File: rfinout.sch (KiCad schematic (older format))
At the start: 4 parts, among them K7 ANT_RLY, P4 ANT, P5 RADIO, P6 PTT_IN

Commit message: All layed out
Several net errors fixed, and some mcu pins reassigned for better layout.
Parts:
- removed K7: ANT_RLY, nu9j-footprints:EC2-12NU, symbol RELAY_2RT
- added K7: ANT_RLY, symbol RELAY_2RT-KEMET
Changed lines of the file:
@@
 Text HLabel 6250 2500 2    60   Output ~ 0
 ptt
+Text Notes 3050 3600 0    60   ~ 0
+SMA Connectors: Johnson 142-0701-801
 $Comp
-L RELAY_2RT K7
-U 1 1 547A886B
+L RELAY_2RT-KEMET K7
+U 1 1 54849E97
 P 6350 3700
 F 0 "K7" H 6300 4100 70  0000 C CNN
 F 1 "ANT_RLY" H 6500 3200 70  0000 C CNN
-F 2 "nu9j-footprints:EC2-12NU" H 6350 3700 60  0001 C CNN
+F 2 "" H 6350 3700 60  0000 C CNN
 F 3 "" H 6350 3700 60  0000 C CNN
 	1    6350 3700
 	1    0    0    -1
 $EndComp
-Text Notes 3050 3600 0    60   ~ 0
-SMA Connectors: Johnson 142-0701-801
 $EndSCHEMATC

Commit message: Connected all mcu VSS and VDD pins.
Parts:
- K7: footprint (none) -> nu9j-footprints:EC2-12NU
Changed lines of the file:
@@
 F 0 "K7" H 6300 4100 70  0000 C CNN
 F 1 "ANT_RLY" H 6500 3200 70  0000 C CNN
-F 2 "" H 6350 3700 60  0000 C CNN
+F 2 "nu9j-footprints:EC2-12NU" H 6350 3700 60  0001 C CNN
 F 3 "" H 6350 3700 60  0000 C CNN
 	1    6350 3700

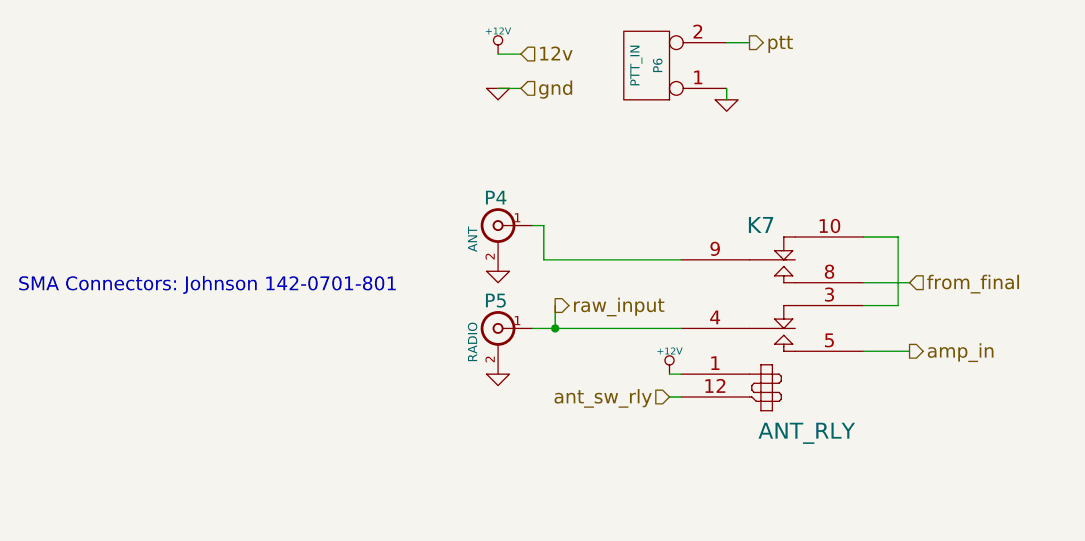
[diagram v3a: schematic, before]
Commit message: Fixed issues found with test board
- Added MOSFETs to relay switch lines from MCU
- Reconnected SWR in/out to actual ADC pins
- Changed LM3940 footprint to SOT223
- Added 4th mounting hole
- Swapped joystick for nav button
- Extended pads of STM32F401 for easier soldering
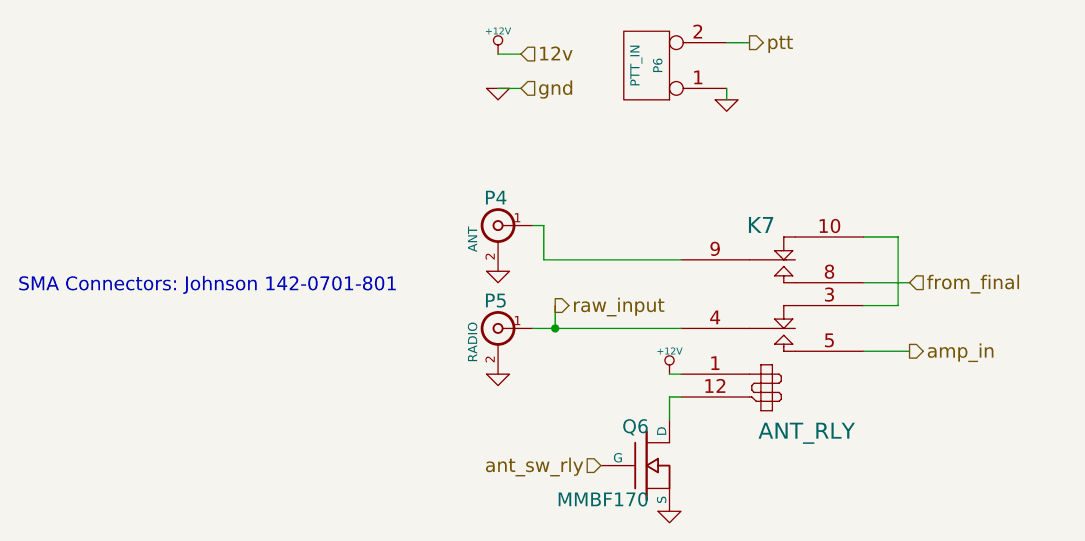
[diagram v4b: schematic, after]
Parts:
- added Q6: MMBF170, nu9j-footprints:sot23-DGS, symbol MOSFET_N
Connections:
- net GND: now also Q6.S
- net ant_sw_rly: now also Q6.G; no longer K7.12
- new net: K7.12, Q6.D
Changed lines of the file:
@@
 $EndComp
 $Comp
-L +12V #PWR098
+L +12V #PWR0101
 U 1 1 5472C39F
 P 5900 3950
-F 0 "#PWR098" H 5900 3900 20  0001 C CNN
+F 0 "#PWR0101" H 5900 3900 20  0001 C CNN
 F 1 "+12V" H 5900 4050 30  0000 C CNN
 F 2 "" H 5900 3950 60  0000 C CNN
@@
 Wire Wire Line
 	5950 4050 5900 4050
-Text HLabel 5900 4050 0    60   Input ~ 0
+Text HLabel 5600 4350 0    60   Input ~ 0
 ant_sw_rly
 $Comp
-L GND #PWR099
+L GND #PWR0102
 U 1 1 5472C3BF
 P 5150 3950
-F 0 "#PWR099" H 5150 3950 30  0001 C CNN
+F 0 "#PWR0102" H 5150 3950 30  0001 C CNN
 F 1 "GND" H 5150 3880 30  0001 C CNN
 F 2 "" H 5150 3950 60  0000 C CNN
@@
 $EndComp
 $Comp
-L GND #PWR0100
+L GND #PWR0103
 U 1 1 5472C3D3
 P 5150 3500
-F 0 "#PWR0100" H 5150 3500 30  0001 C CNN
+F 0 "#PWR0103" H 5150 3500 30  0001 C CNN
 F 1 "GND" H 5150 3430 30  0001 C CNN
 F 2 "" H 5150 3500 60  0000 C CNN
@@
 from_final
 $Comp
-L GND #PWR0101
+L GND #PWR0104
 U 1 1 5472C7C7
 P 5150 2700
-F 0 "#PWR0101" H 5150 2700 30  0001 C CNN
+F 0 "#PWR0104" H 5150 2700 30  0001 C CNN
 F 1 "GND" H 5150 2630 30  0001 C CNN
 F 2 "" H 5150 2700 60  0000 C CNN
@@
 $EndComp
 $Comp
-L +12V #PWR0102
+L +12V #PWR0105
 U 1 1 5472C7D2
 P 5150 2550
-F 0 "#PWR0102" H 5150 2500 20  0001 C CNN
+F 0 "#PWR0105" H 5150 2500 20  0001 C CNN
 F 1 "+12V" H 5150 2650 30  0000 C CNN
 F 2 "" H 5150 2550 60  0000 C CNN
@@
 $EndComp
 $Comp
-L GND #PWR0103
+L GND #PWR0106
 U 1 1 5472CC45
 P 6150 2750
-F 0 "#PWR0103" H 6150 2750 30  0001 C CNN
+F 0 "#PWR0106" H 6150 2750 30  0001 C CNN
 F 1 "GND" H 6150 2680 30  0001 C CNN
 F 2 "" H 6150 2750 60  0000 C CNN
@@
 	1    0    0    -1
 $EndComp
+$Comp
+L MOSFET_N Q6
+U 1 1 54C4737E
+P 5800 4350
+F 0 "Q6" H 5810 4520 60  0000 R CNN
+F 1 "MMBF170" H 5810 4200 60  0000 R CNN
+F 2 "nu9j-footprints:sot23-DGS" H 5800 4350 60  0001 C CNN
+F 3 "" H 5800 4350 60  0000 C CNN
+	1    5800 4350
+	1    0    0    -1
+$EndComp
+Wire Wire Line
+	5900 4050 5900 4150
+$Comp
+L GND #PWR0107
+U 1 1 54C473D2
+P 5900 4550
+F 0 "#PWR0107" H 5900 4550 30  0001 C CNN
+F 1 "GND" H 5900 4480 30  0001 C CNN
+F 2 "" H 5900 4550 60  0000 C CNN
+F 3 "" H 5900 4550 60  0000 C CNN
+	1    5900 4550
+	1    0    0    -1
+$EndComp

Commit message: Schematic changes to go with #3 (extending sot23 pads)
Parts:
- Q6: footprint nu9j-footprints:sot23-DGS -> nu9j-footprints:SOT-23-DGS_HandSoldering
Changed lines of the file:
@@
 F 0 "Q6" H 5810 4520 60  0000 R CNN
 F 1 "MMBF170" H 5810 4200 60  0000 R CNN
-F 2 "nu9j-footprints:sot23-DGS" H 5800 4350 60  0001 C CNN
+F 2 "nu9j-footprints:SOT-23-DGS_HandSoldering" H 5800 4350 60  0001 C CNN
 F 3 "" H 5800 4350 60  0000 C CNN
 	1    5800 4350
